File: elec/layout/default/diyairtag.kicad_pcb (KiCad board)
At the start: 2 copper layers, 40 x 40 mm, 0 parts

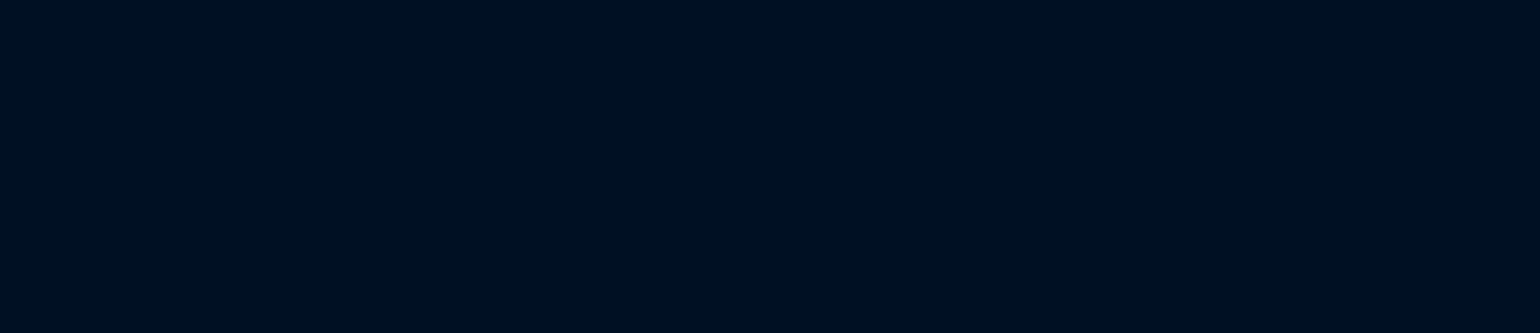
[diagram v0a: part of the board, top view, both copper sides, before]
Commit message: fixed adjacent
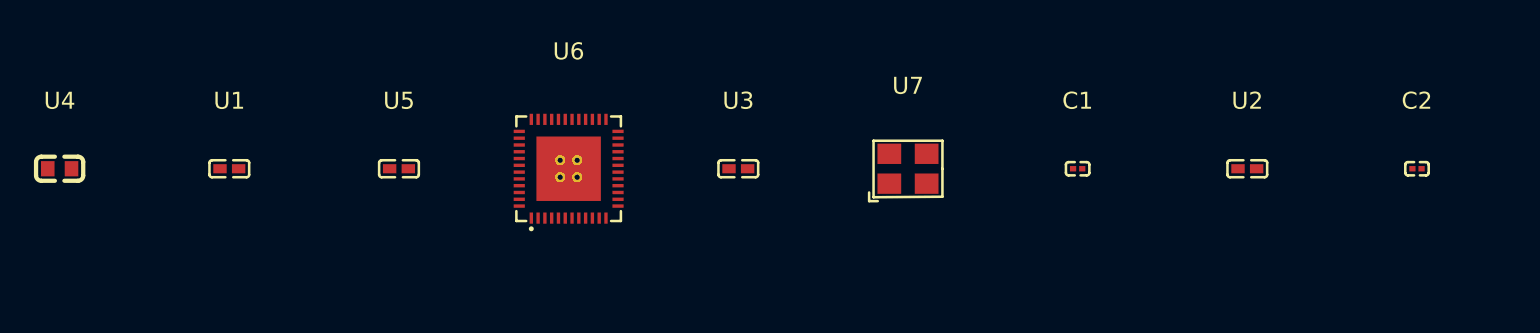
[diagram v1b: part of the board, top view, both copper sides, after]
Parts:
- added C1: , atopile:C0201-a4ec75, F.Cu at (70.0, -5.00)
- added C2: , atopile:C0201-a4ec75, F.Cu at (90.0, -5.00)
- added U1: 1nF ±10% 50V X7R, atopile:C0402-b3ef17, F.Cu at (20.0, -5.00)
- added U2: 100nF ±10% 16V X7R, atopile:C0402-b3ef17, F.Cu at (80.0, -5.00)
- added U3: 47nF ±10% 50V X7R, atopile:C0402-b3ef17, F.Cu at (50.0, -5.00)
- added U4: 4.7µF ±10% 10V X5R, atopile:C0603-bd72f6, F.Cu at (10.0, -5.00)
- added U5: 100nF ±10% 16V X7R, atopile:C0402-b3ef17, F.Cu at (30.0, -5.00)
- added U6: , lib:QFN-48_L6.0-W6.0-P0.40-BL-EP3.8, F.Cu at (40.0, -5.00)
- added U7: , lib:OSC-SMD_4P-L3.2-W2.5-BL, F.Cu at (60.0, -5.00)
